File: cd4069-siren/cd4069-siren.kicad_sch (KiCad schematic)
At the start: 13 parts, among them Q1 NPN, U1 4069

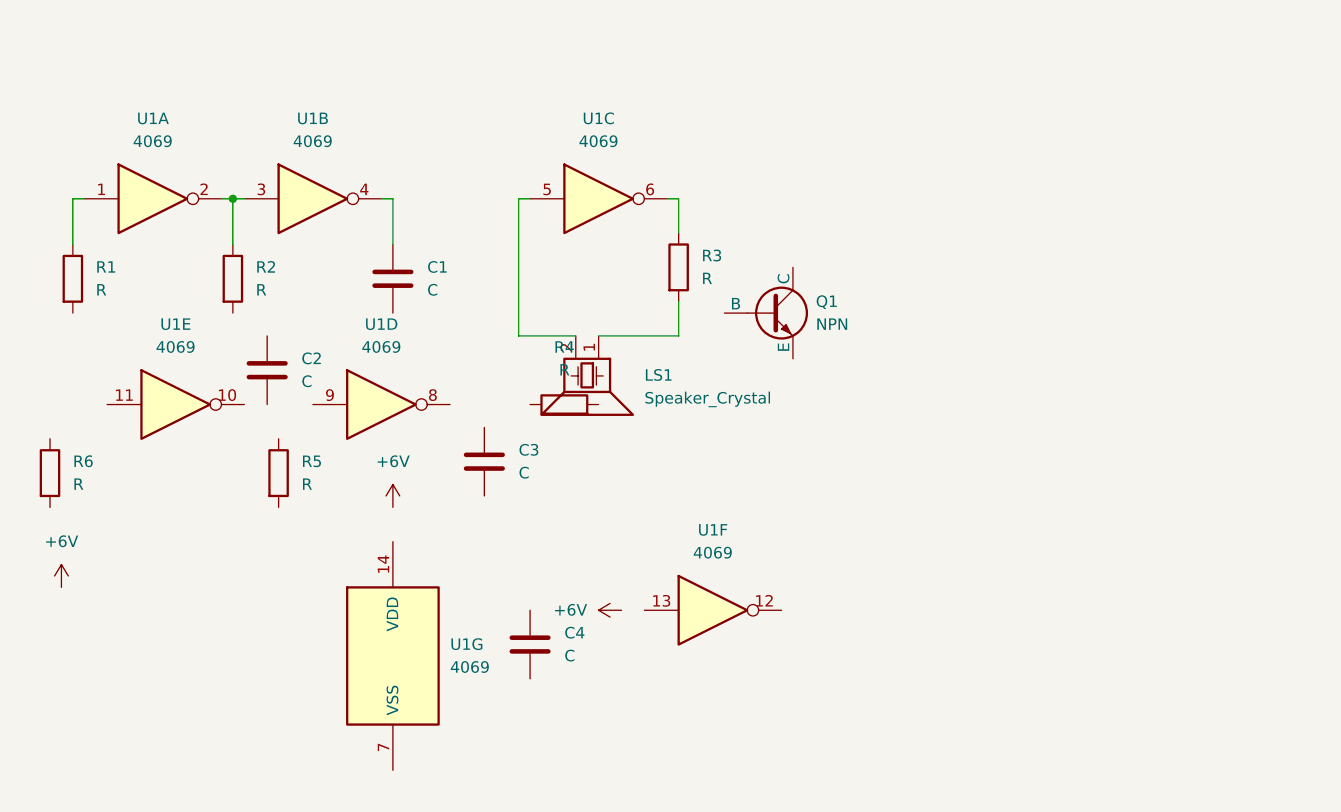
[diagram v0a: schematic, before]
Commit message: project 7 / cd4069 siren / added footprints and designed layout for pcb components
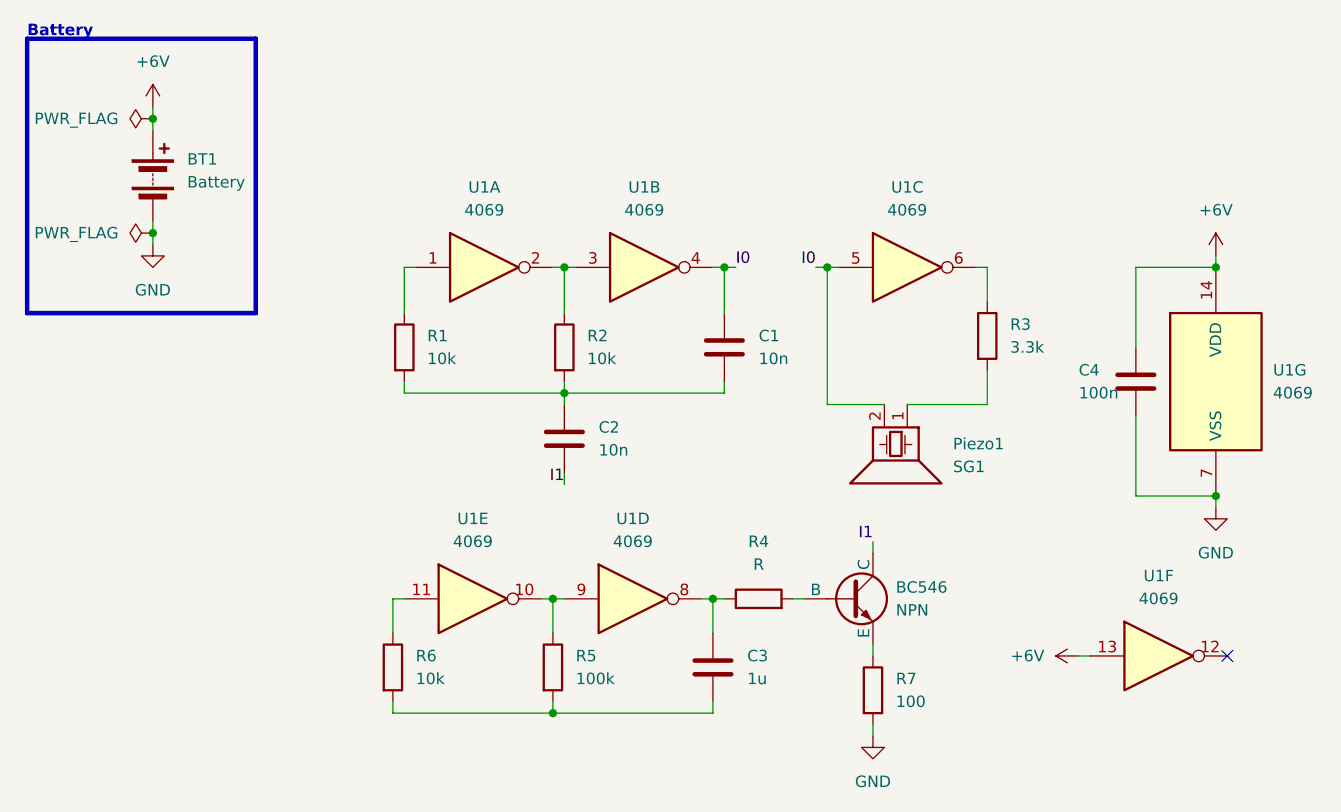
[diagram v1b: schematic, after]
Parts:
- added BT1: Battery, Connector_PinHeader_2.54mm:PinHeader_1x02_P2.54mm_Vertical, symbol Device:Battery
- added R7: 100, Resistor_THT:R_Axial_DIN0204_L3.6mm_D1.6mm_P7.62mm_Horizontal, symbol Device:R
- BC546: renamed from Q1; footprint (none) -> Package_TO_SOT_THT:TO-92
- C1, C2: value C -> 10n; footprint (none) -> Capacitor_THT:C_Disc_D3.0mm_W1.6mm_P2.50mm
- C3: value C -> 1u; footprint (none) -> Capacitor_THT:C_Disc_D3.0mm_W1.6mm_P2.50mm
- C4: value C -> 100n; footprint (none) -> Capacitor_THT:C_Disc_D3.0mm_W1.6mm_P2.50mm
- Piezo1: renamed from LS1; value Speaker_Crystal -> SG1; footprint (none) -> Buzzer_Beeper:Buzzer_12x9.5RM7.6
- R1, R2, R6: value R -> 10k; footprint (none) -> Resistor_THT:R_Axial_DIN0204_L3.6mm_D1.6mm_P7.62mm_Horizontal
- R3: value R -> 3.3k; footprint (none) -> Resistor_THT:R_Axial_DIN0204_L3.6mm_D1.6mm_P7.62mm_Horizontal
- R4: footprint (none) -> Resistor_THT:R_Axial_DIN0204_L3.6mm_D1.6mm_P7.62mm_Horizontal
- R5: value R -> 100k; footprint (none) -> Resistor_THT:R_Axial_DIN0204_L3.6mm_D1.6mm_P7.62mm_Horizontal
- U1: footprint (none) -> Package_DIP:DIP-14_W7.62mm
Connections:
- net +6V: now also C4.1, U1.13, U1.14 (VDD), BT1.1 (+)
- net GND: now reaches C4.2
- net GND: now also U1.7 (VSS), BT1.2 (-), R7.2
- net I0: now reaches Piezo1.2, U1.5
- net I0: now also C1.1, U1.4
- net at C1.2: now also C2.1, R1.2, R2.2
- net I1: now reaches BC546.1 (C)
- net I1: now also C2.2
- net at BC546.2 (B): now also R4.2
- net at BC546.3 (E): now also R7.1
- net at U1.8: now also C3.1, R4.1
- net at U1.9: now also R5.1, U1.10
- net at R6.1: now also U1.11
- net at R6.2: now also C3.2, R5.2
- no-connect marks 0 -> 1
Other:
- note added: "Battery"
- moved on the sheet: BC546, C1, C2, C3, C4, Piezo1, R1, R2, R3, R4, R5, R6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
